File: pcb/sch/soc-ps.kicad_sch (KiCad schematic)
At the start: 11 parts, among them U1 XC7Z020CLG484

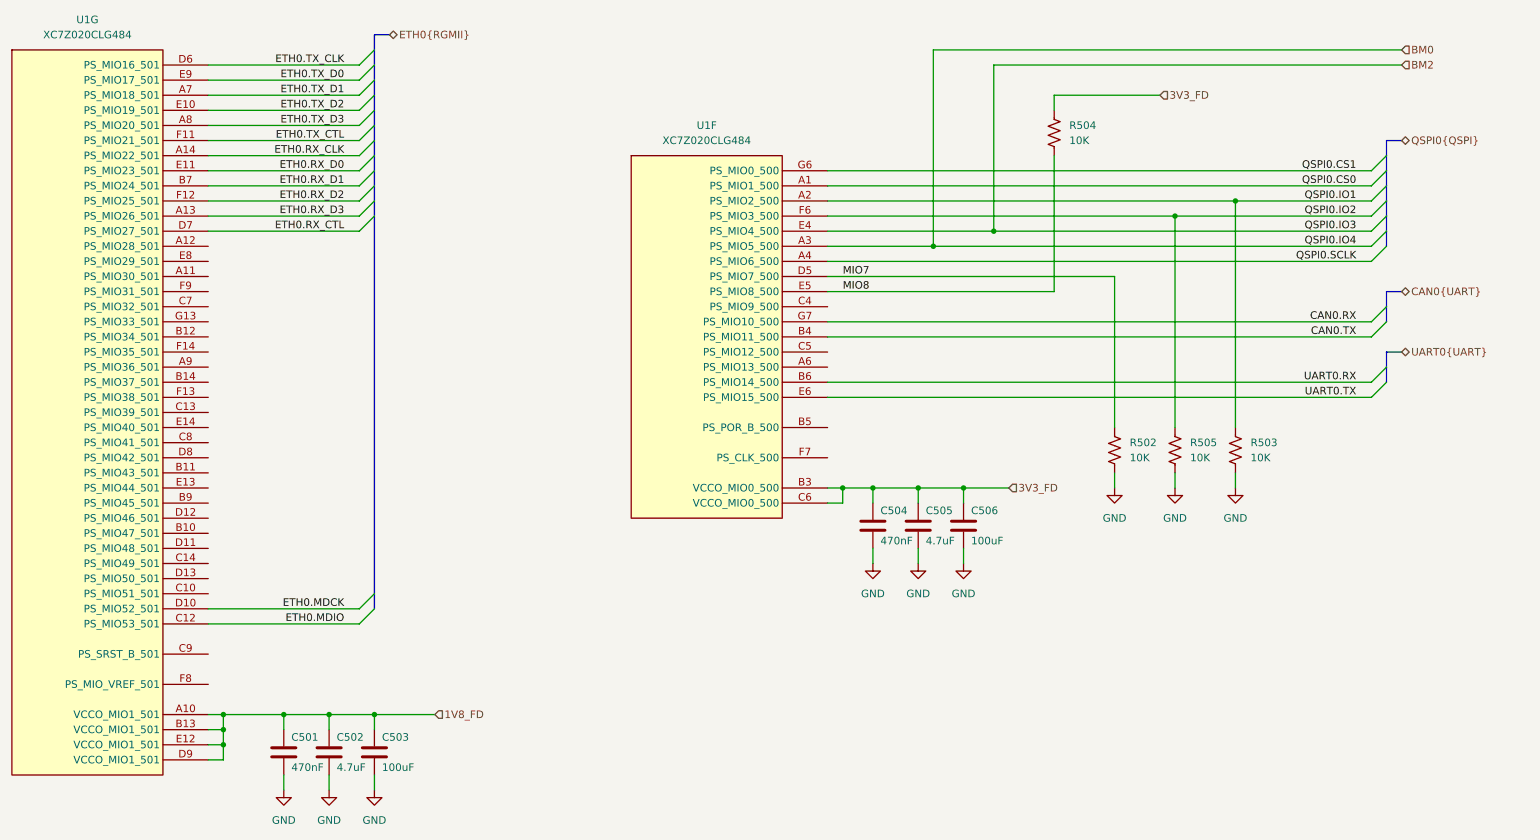
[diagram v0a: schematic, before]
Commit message: fices for boot definition
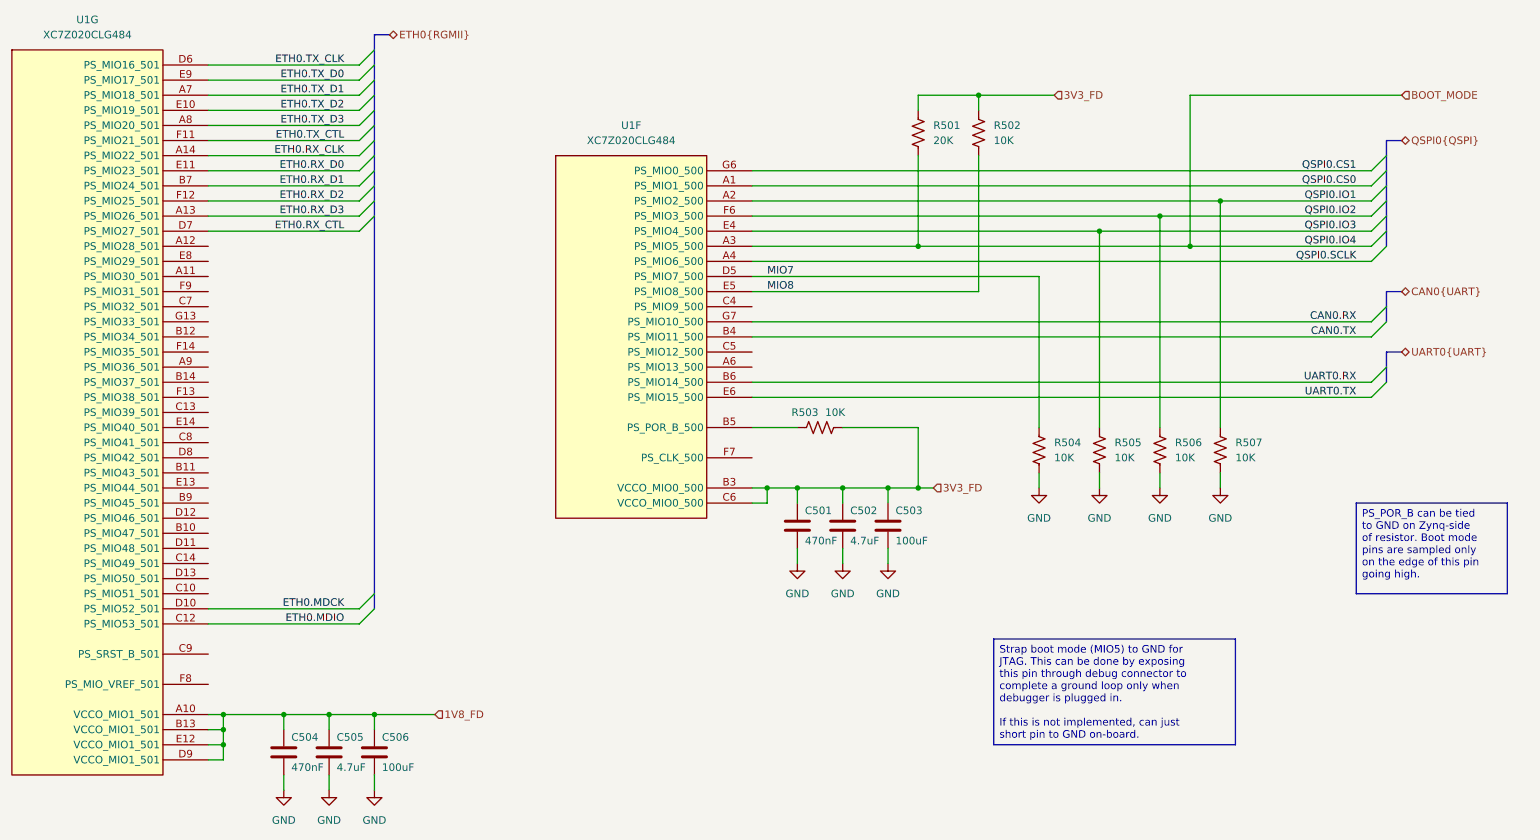
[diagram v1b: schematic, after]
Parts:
- added R501: 20K, Resistor_SMD:R_0402_1005Metric, symbol Device:R_US
- added R503, R505: 10K, Resistor_SMD:R_0402_1005Metric, symbol Device:R_US
- renumbered C504 to C501, C505 to C502, C506 to C503, C501 to C504, C502 to C505, C503 to C506, R504 to R502, R502 to R504, R505 to R506, R503 to R507
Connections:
- net 3V3_FD: now also R501.1, R503.2
- net GND: now also R505.2
- net at U1.B5 (PS_POR_B_500): now also R503.1
- net BM0 renamed BOOT_MODE
- net BOOT_MODE: now also R501.2
- net BM2 renamed QSPI0.IO3
- net QSPI0.IO3: now also R505.1
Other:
- moved on the sheet: C501, C502, C503, R502, R504, R506, R507, U1F

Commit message: power
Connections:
- net 1V8_FD renamed 1V8_Z
- net 3V3_FD renamed 3V3_Z
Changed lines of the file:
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@@
 	)
 	(junction
-		(at 175.26 104.14)
-		(diameter 0)
-		(color 0 0 0 0)
-	)
-	(junction
 		(at 162.56 104.14)
 		(diameter 0)
@@
 	)
 	(junction
+		(at 175.26 104.14)
+		(diameter 0)
+		(color 0 0 0 0)
+	)
+	(junction
 		(at 220.98 63.5)
 		(diameter 0)
@@
 	(wire
 		(pts
-			(xy 175.26 104.14) (xy 177.8 104.14)
+			(xy 175.26 104.14) (xy 180.34 104.14)
 		)
 		(stroke
@@
 		)
 	)
-	(hierarchical_label "1V8_FD"
+	(hierarchical_label "1V8_Z"
 		(shape input)
 		(at 93.98 142.24 0)
@@
 		)
 	)
-	(hierarchical_label "3V3_FD"
+	(hierarchical_label "3V3_Z"
 		(shape input)
-		(at 177.8 104.14 0)
+		(at 180.34 104.14 0)
 		(effects
 			(font
@@
 		)
 	)
-	(hierarchical_label "3V3_FD"
+	(hierarchical_label "3V3_Z"
 		(shape input)
 		(at 198.12 38.1 0)
